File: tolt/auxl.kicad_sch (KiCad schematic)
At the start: 2 parts, among them U17 BMI160, U18 ESP32-C3_SUPERMINI_SMD

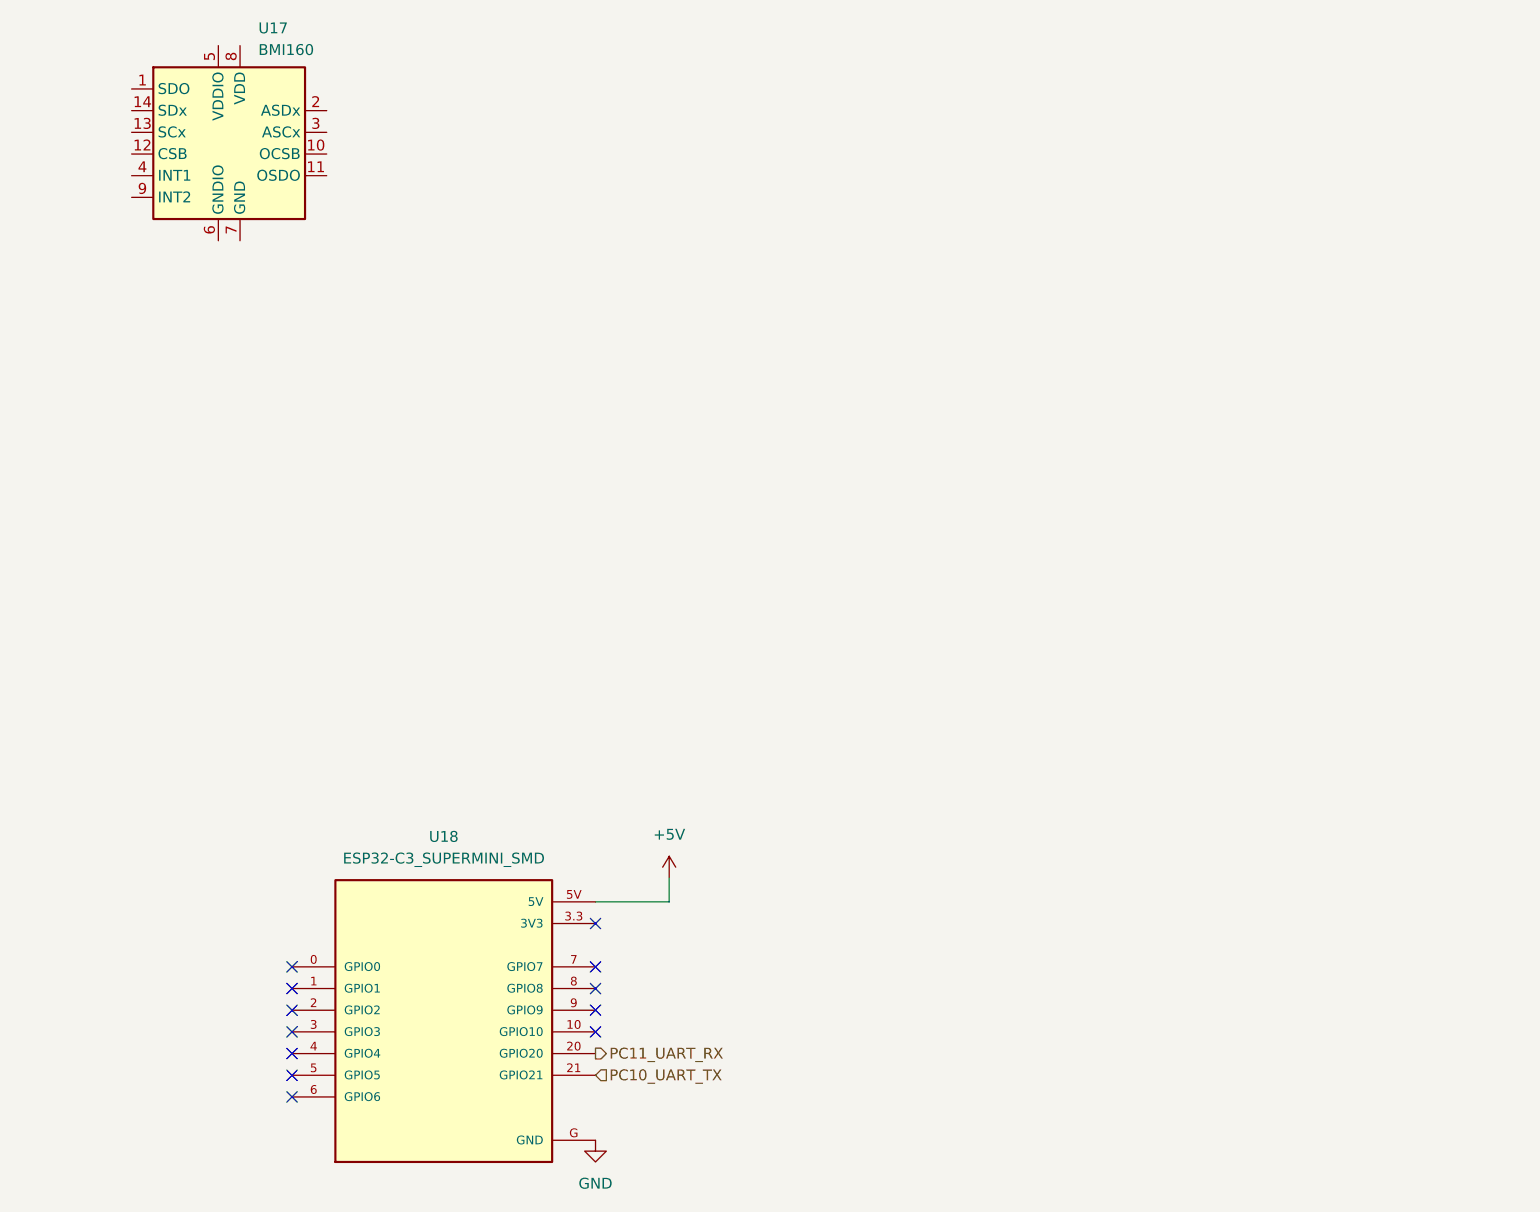
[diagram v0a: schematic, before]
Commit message: modified:   tolt/auxl.kicad_sch 	modified:   tolt/converters.kicad_sch 	modified:   tolt/powerstage.kicad_sch 	modified:   tolt/stm32.kicad_sch 	modified:   tolt/tolt.kicad_pcb 	modified:   tolt/tolt.kicad_pro 	modified:   tolt/tolt.kicad_sch 	SOP120P1500X235-17N.step 	tolt/Library.pretty/HDSOP-16-2.kicad_mod 	tolt/Library.pretty/R5930.kicad_mod 	tolt/conn.kicad_sch
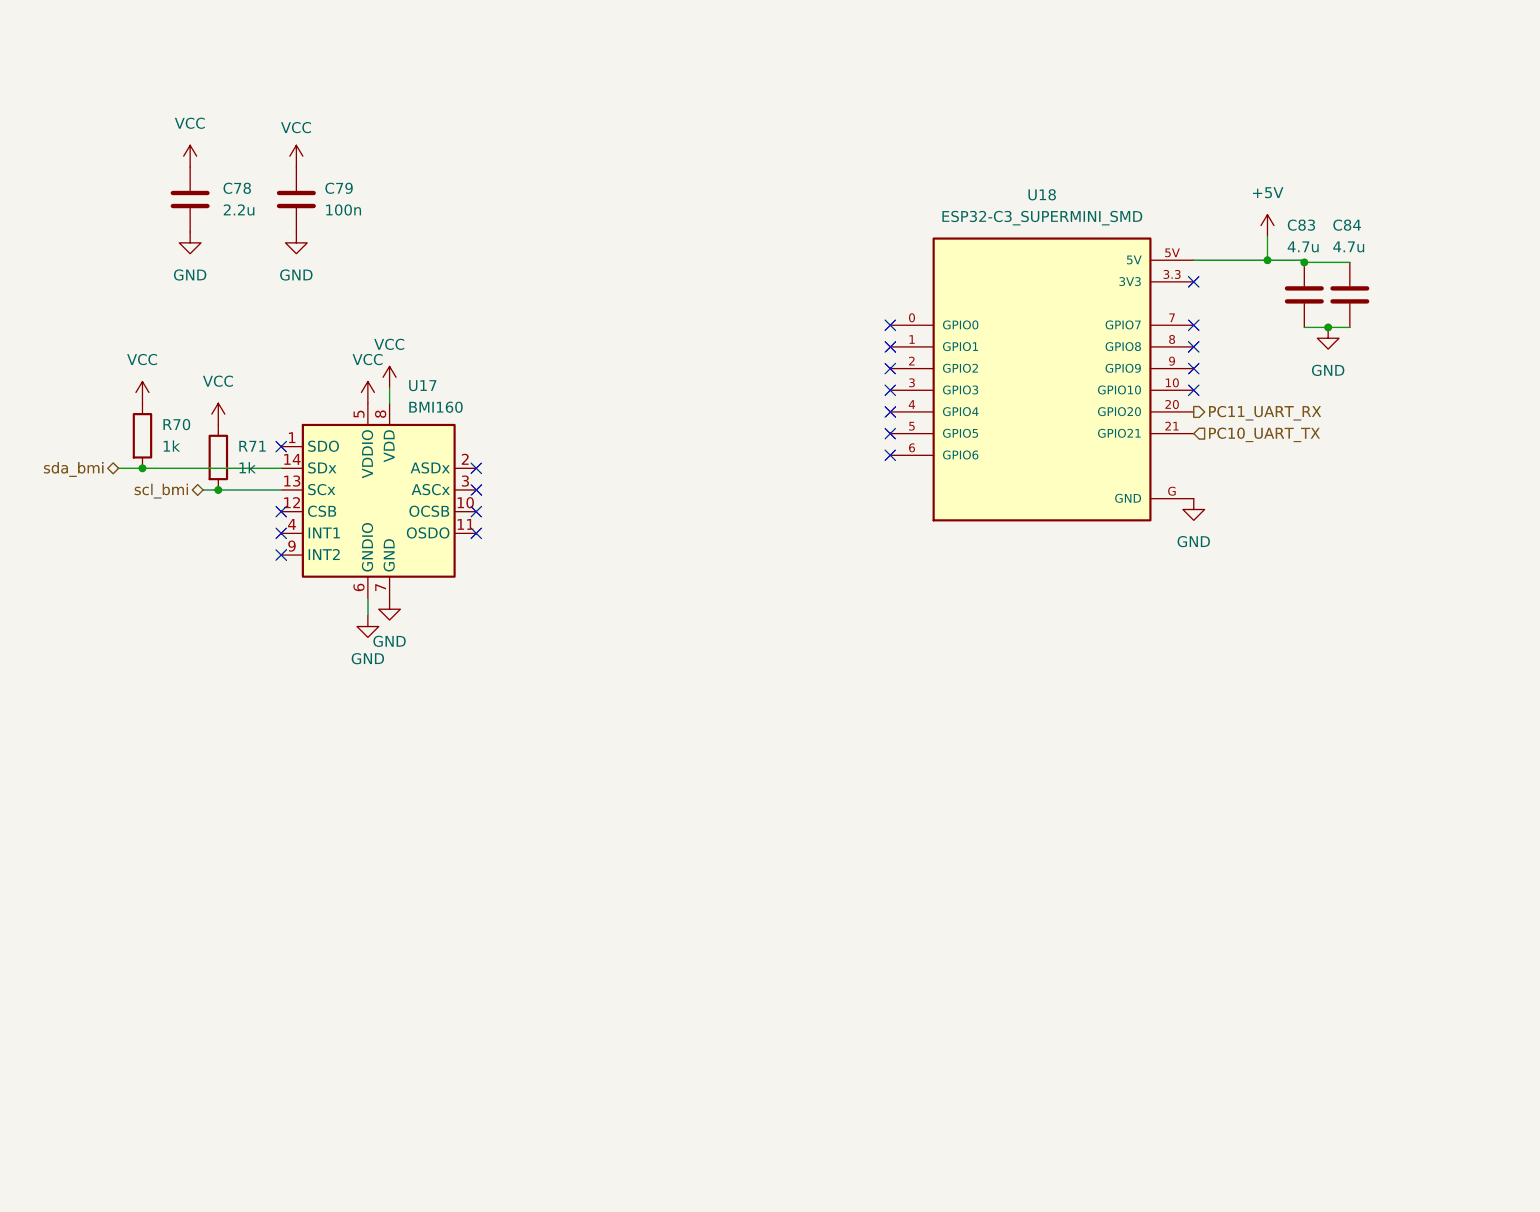
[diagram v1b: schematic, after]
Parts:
- added C78: 2.2u, Capacitor_SMD:C_0603_1608Metric, symbol Device:C
- added C79: 100n, Capacitor_SMD:C_0402_1005Metric, symbol Device:C
- added C83, C84: 4.7u, Capacitor_SMD:C_0805_2012Metric, symbol Device:C
- added R70, R71: 1k, Resistor_SMD:R_0603_1608Metric, symbol Device:R
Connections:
- net +5V: now also C83.2, C84.2
- net GND: now also U17.6 (GNDIO), U17.7 (GND), C78.1, C79.1, C83.1, C84.1
- net scl_bmi: now reaches U17.13 (SCx)
- net scl_bmi: now also R71.2
- net sda_bmi: now reaches U17.14 (SDx)
- net sda_bmi: now also R70.2
- net VCC: now reaches U17.5 (VDDIO)
- net VCC: now also U17.8 (VDD), C78.2, C79.2, R70.1, R71.1
- no-connect marks 12 -> 20
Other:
- moved on the sheet: U17, U18

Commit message: new file:   tolt/Library.pretty/IND-SMD_L3.9-W3.9-1.kicad_mod 	new file:   tolt/Library.pretty/IND-SMD_L5.0-W5.0.kicad_mod 	modified:   tolt/auxl.kicad_sch 	modified:   tolt/conn.kicad_sch 	modified:   tolt/converters.kicad_sch 	new file:   tolt/fp-lib-table 	modified:   tolt/inter.kicad_sch 	modified:   tolt/powerstage.kicad_sch 	modified:   tolt/stm32.kicad_sch 	modified:   tolt/tolt.kicad_sch
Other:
- moved on the sheet: C78, C79, R70, R71, U17

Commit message: new file:   tolt/Library.pretty/PQDE6W.kicad_mod 	modified:   tolt/auxl.kicad_sch 	modified:   tolt/conn.kicad_sch 	modified:   tolt/converters.kicad_sch 	modified:   tolt/powerstage.kicad_sch 	modified:   tolt/tolt.kicad_pcb 	modified:   tolt/tolt.kicad_sch
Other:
- moved on the sheet: C83, C84, R70, R71, U17, U18

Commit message: move comp
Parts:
- removed C83, C84: 4.7u, Capacitor_SMD:C_0805_2012Metric, symbol Device:C
- removed U18: ESP32-C3_SUPERMINI_SMD, Library:MODULE_ESP32-C3_SUPERMINI, symbol ESP32-C3_SUPERMINI_SMD:ESP32-C3_SUPERMINI_SMD
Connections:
- no-connect marks 20 -> 8

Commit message: .
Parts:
- added J16, J17: NRST, Jumper:SolderJumper-2_P1.3mm_Open_RoundedPad1.0x1.5mm, symbol Connector_Generic:Conn_01x02
- added R112, R113: 10k, Resistor_SMD:R_0603_1608Metric, symbol Device:R_Small
- added U18: ESP32-C3-WROOM-02, PCM_Espressif:ESP32-C3-WROOM-02, symbol PCM_Espressif:ESP32-C3-WROOM-02
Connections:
- net GND: now also J16.1 (Pin_1), J17.1 (Pin_1), U18.19 (GND), U18.9 (GND)
- net VCC: now also R112.1, R113.1, U18.1 (3V3)
- new net: J16.2 (Pin_2), R112.2, U18.2 (EN/CHIP_PU)
- new net: J17.2 (Pin_2), R113.2, U18.8 (GPIO9)
- new net ESP_D+: U18.14 (GPIO19/USB_D+)
- new net ESP_D-: U18.13 (GPIO18/USB_D-)

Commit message: FINAL?
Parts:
- added J13: Conn_01x04, Connector_JST:JST_PH_B4B-PH-K_1x04_P2.00mm_Vertical, symbol Connector_Generic:Conn_01x04
- added TP1, TP10, TP11, TP12, TP2, TP3, TP4, TP5, TP6, TP7, TP8, TP9: TestPoint, TestPoint:TestPoint_Pad_D1.0mm, symbol Connector:TestPoint
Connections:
- net GND: now also J13.1 (Pin_1)
- net PC10_UART_TX: now also J13.3 (Pin_3)
- net PC11_UART_RX: now also J13.2 (Pin_2)
- net at U18.10 (GPIO10): now also TP10.1
- net at U18.11 (GPIO20/U0RXD): now also TP1.1
- net at U18.12 (GPIO21/U0TXD): now also TP2.1
- net at U18.15 (GPIO3/ADC1_CH3): now also TP4.1
- net at U18.16 (GPIO2/ADC1_CH2): now also TP3.1
- net at U18.17 (GPIO1/ADC1_CH1/XTAL_32K_N): now also TP12.1
- net at U18.18 (GPIO0/ADC1_CH0/XTAL_32K_P): now also TP11.1
- net at U18.3 (GPIO4/ADC1_CH4): now also TP5.1
- net at U18.4 (GPIO5/ADC2_CH0): now also TP6.1
- net at U18.5 (GPIO6): now also TP7.1
- net at U18.6 (GPIO7): now also TP8.1
- net at U18.7 (GPIO8): now also TP9.1
- new net +5V: J13.4 (Pin_4)

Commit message: FINAL
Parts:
- C78: LCSC (none) -> C913904
- C79: LCSC (none) -> C60474
- J16, J17: now fitted
- R70, R71: LCSC (none) -> C2907114
- U17: value BMI160 -> BMI323; LCSC (none) -> C5368700
